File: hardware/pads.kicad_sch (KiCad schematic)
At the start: 56 parts, among them J1 5V, J10 5V, J11 5V, J12 5V, J13 5V, J14 5V, J15 5V, J16 5V, J17 5V, J18 5V, J19 5V, J2 5V, J20 5V, J21 5V, J22 5V, J23 5V, J24 5V, J25 5V, J26 5V, J27 5V, J28 5V, J29 5V, J3 5V, J30 5V, J31 5V, J32 5V, J33 5V, J34 5V, J35 5V, J36 5V, J37 5V, J38 5V, J39 5V, J4 5V, J40 5V, J41 5V, J42 5V, J43 5V, J44 5V, J45 5V, J46 5V, J47 5V, J48 5V, J49 5V, J5 5V, J50 5V, J51 5V, J52 5V, J53 5V, J54 5V, J6 5V, J7 5V, J8 5V, J9 5V, P1 SM08B-SRSS-TB(LF)(SN), U8 SM06B-SRSS-TB(LF)(SN)

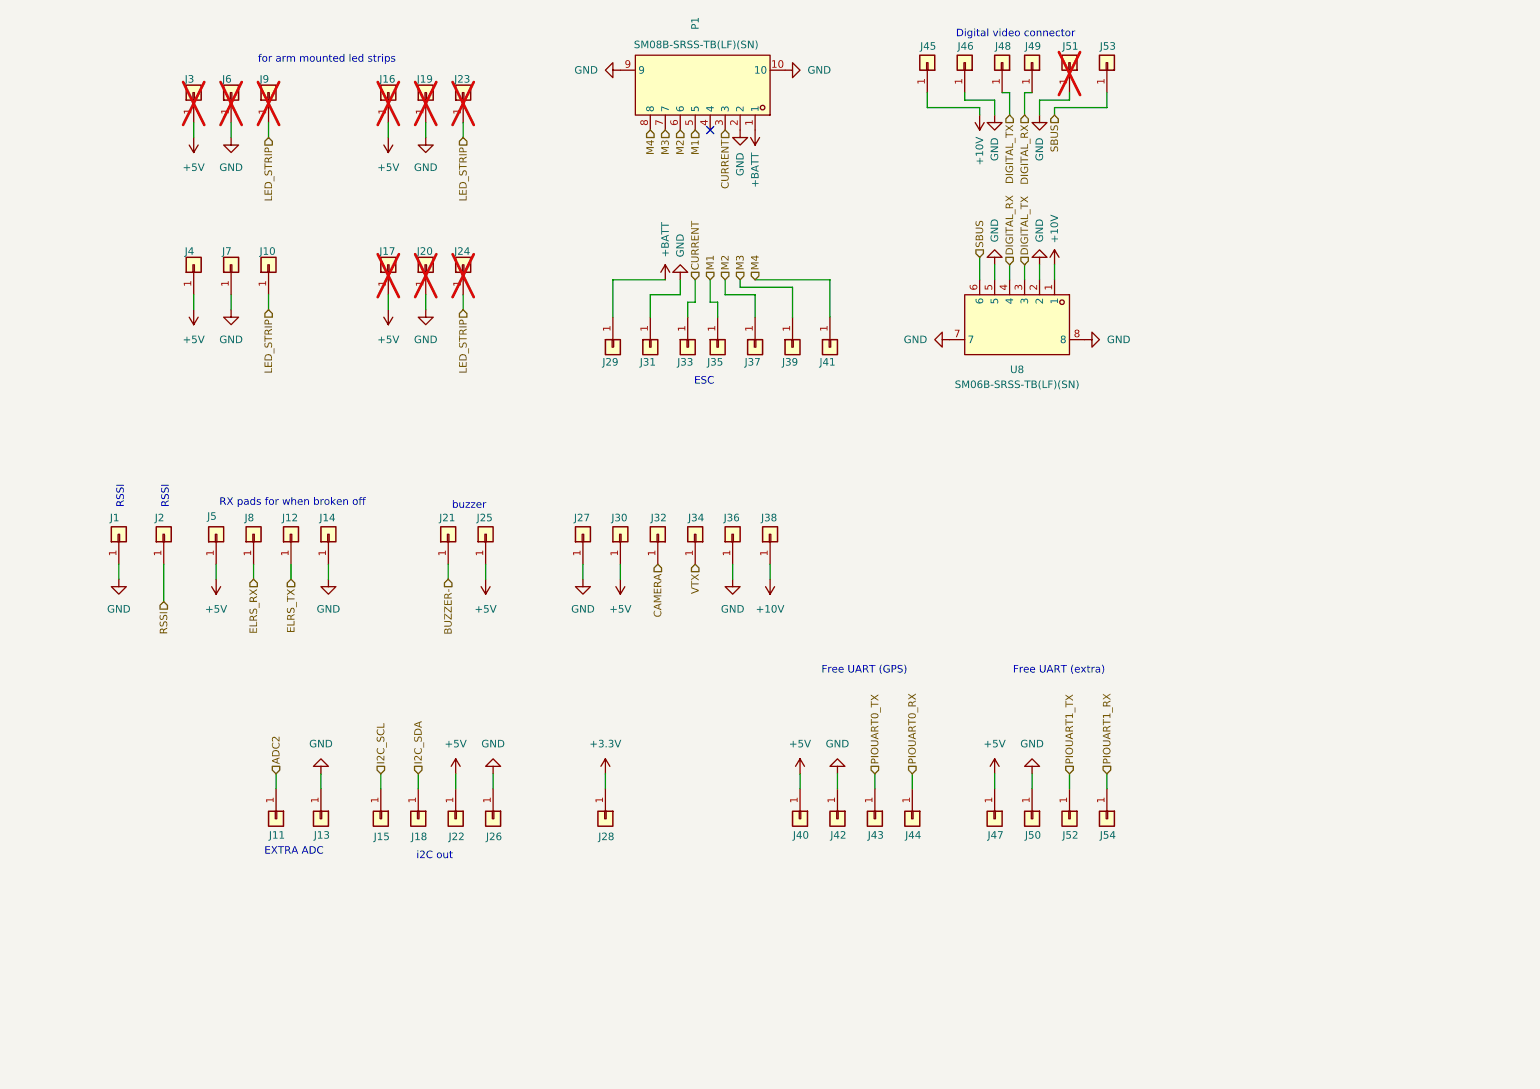
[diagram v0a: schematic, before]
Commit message: Rev 2 (RP2354A): finalize design, update docs, clean repo (#5)
* docs(readme): add analog OSD BOM to Rev 2 change list

Document OSD debugging findings and component changes as a new
Analog OSD section in the Rev 2 Change List:
- HW-12: U19 op-amp TLV9061IDPWR -> COS8051SOT (175MHz video-grade RRIO)
- HW-13: output front-end add AC-couple + DC-restore, power U19 from +5V
- HW-14: U20 comparator TLV3201AIDBVR -> TLV7031DPWR (push-pull, X2SON, ~75% smaller)
- HW-15: add OSD_EN select pull-down (datasheet-required, defaults to pass-through)
- U18 / D9 verified correct, no change; OSD GPIO mapping noted (PA4/5/6)

Also fix HW-11 beeper GPIO: GPIO6 -> GPIO7 (GPIO6 is OSD_SYNC per netlist).

Co-Authored-By: Claude Opus 4.8 (1M context) <noreply@anthropic.com>

* many tiny improvements

- I/O correctness
- SPI0/SPI1/I2C0 bus corrections
- decoupling of DVDD
- ADC_AVDD as per RPi documents
- removal of SBUS
- connect ESC serial
- remove RUN RC-circuit as per RPi documentation
- some more cleanup for readability
- gyro CLKIN decision
- I2C 4.7k pullup

* RP2354A

* piu1

* switch spi

* Update OpenFC.kicad_pcb

* routex2

* some minor tweaks

- remove some unnecessary resistors
- slightly higher 10V rail to account for voltage drop
- some cleanup
- simpler PG 1.8V circuit

* Update imu.kicad_sch

* LED resistors

Also reduced the amount of different resistors for cheaper assembly

* Delete leds.kicad_sch

* remove some unneeded decoupling caps from RP2350

* update MOSFET part numbers

* OSD

* ROUTE

* clean libs

* details

* led names

* Clean routing

* docs: rewrite README + CLAUDE.md for finalized Rev 2 (RP2354A)

Rev 2 is a substantial redesign that the docs no longer matched. Updated
both to the actual schematic, verified from the current netlist:

- MCU: RP2354B (QFN-80, GPIO0-47) -> RP2354A (QFN-60, GPIO0-29). Full GPIO
  map re-derived from the netlist + QFN-60 pinout; all 30 GPIO documented.
- IMU moved to SPI1, microSD to SPI0; ref designators re-annotated
  (op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
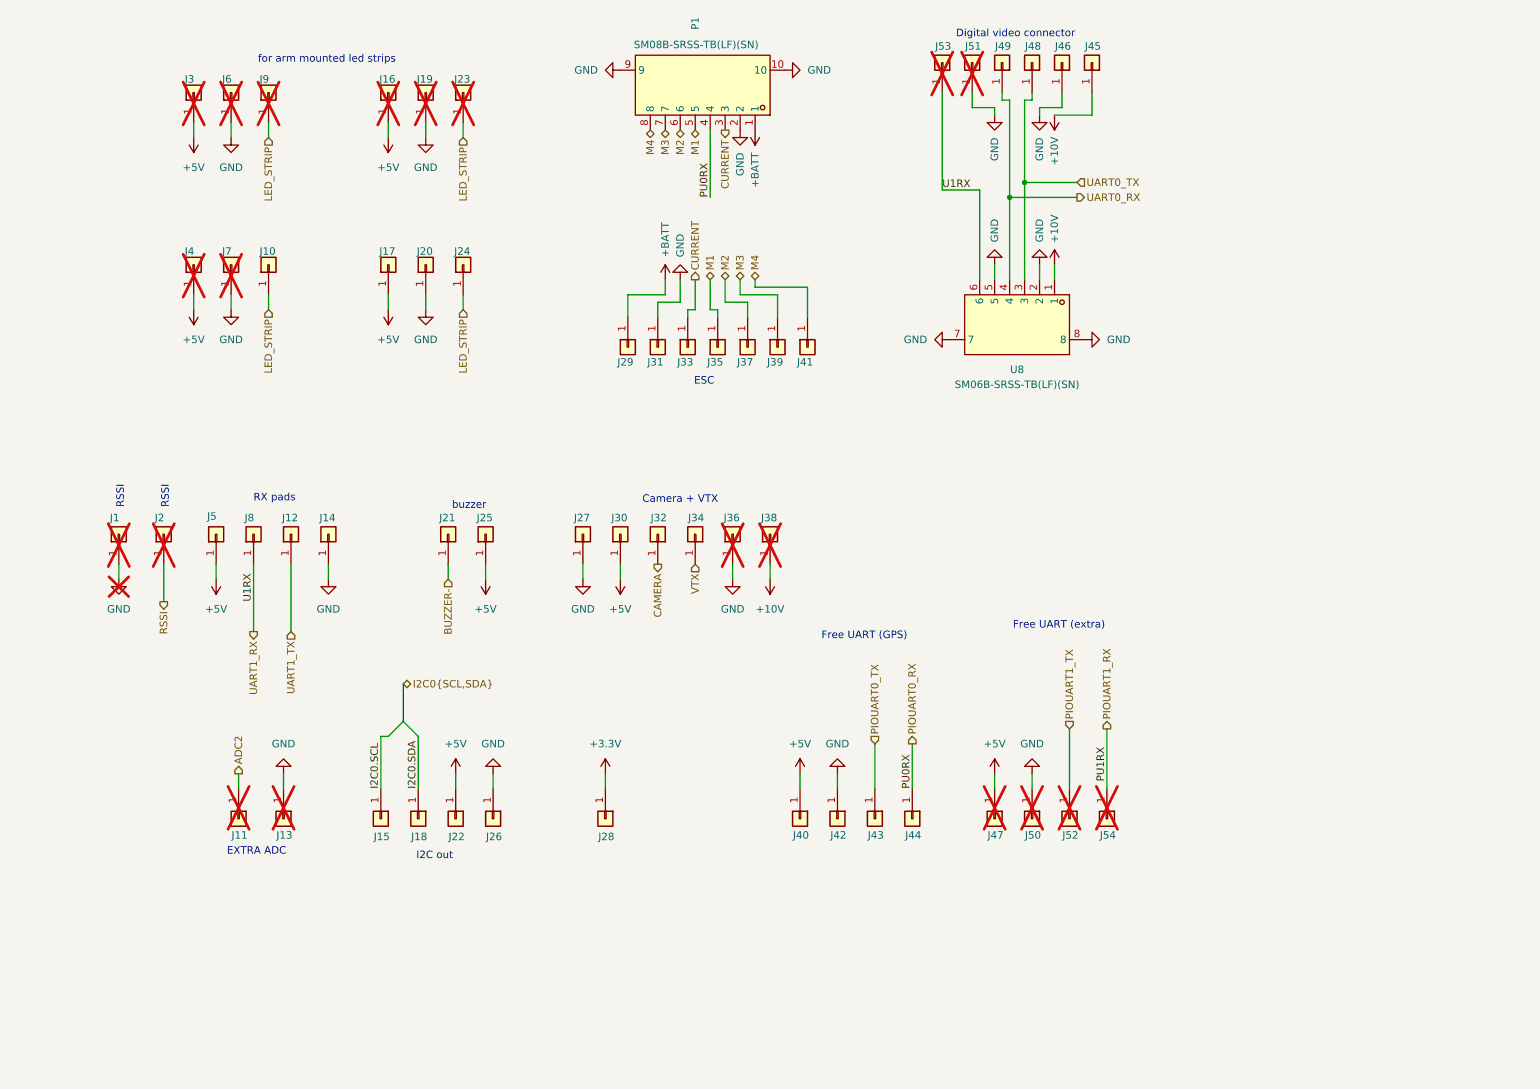
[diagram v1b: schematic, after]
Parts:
- J1, J11, J13, J2, J36, J38, J4, J47, J50, J52, J53, J54, J7: now not fitted
- J17, J20, J24: now fitted; now in the parts list
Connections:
- net SBUS is gone; now on net UART1_RX: J53.1 (Pin_1), U8.6
- net PIOUART0_RX: now also P1.4
- net DIGITAL_RX renamed UART0_RX
- net DIGITAL_TX renamed UART0_TX
- net ELRS_RX renamed UART1_RX
- net ELRS_TX renamed UART1_TX
- net I2C_SCL renamed I2C0.SCL
- net I2C_SDA renamed I2C0.SDA
- no-connect marks 1 -> 0
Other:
- note added: "Camera + VTX"
- note added: "I2C out"
- note added: "RX pads"
- note removed: "RX pads for when broken off"
- note removed: "i2C out"
- moved on the sheet: J29, J31, J37, J39, J41, J45, J46, J48, J49, J51

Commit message: docs(schematic): add design annotations to all sheets
Port on-canvas engineering comments from OpenFC-Lite (RP2354B), adapted to the
Mini layout. +41 text items across root, rp2350a, power, imu, osd, blackbox,
pads. Annotation/text only — no net or connectivity changes. Mirrors
hardware/DESIGN_NOTES.md.

Co-Authored-By: Claude Opus 4.8 (1M context) <noreply@anthropic.com>
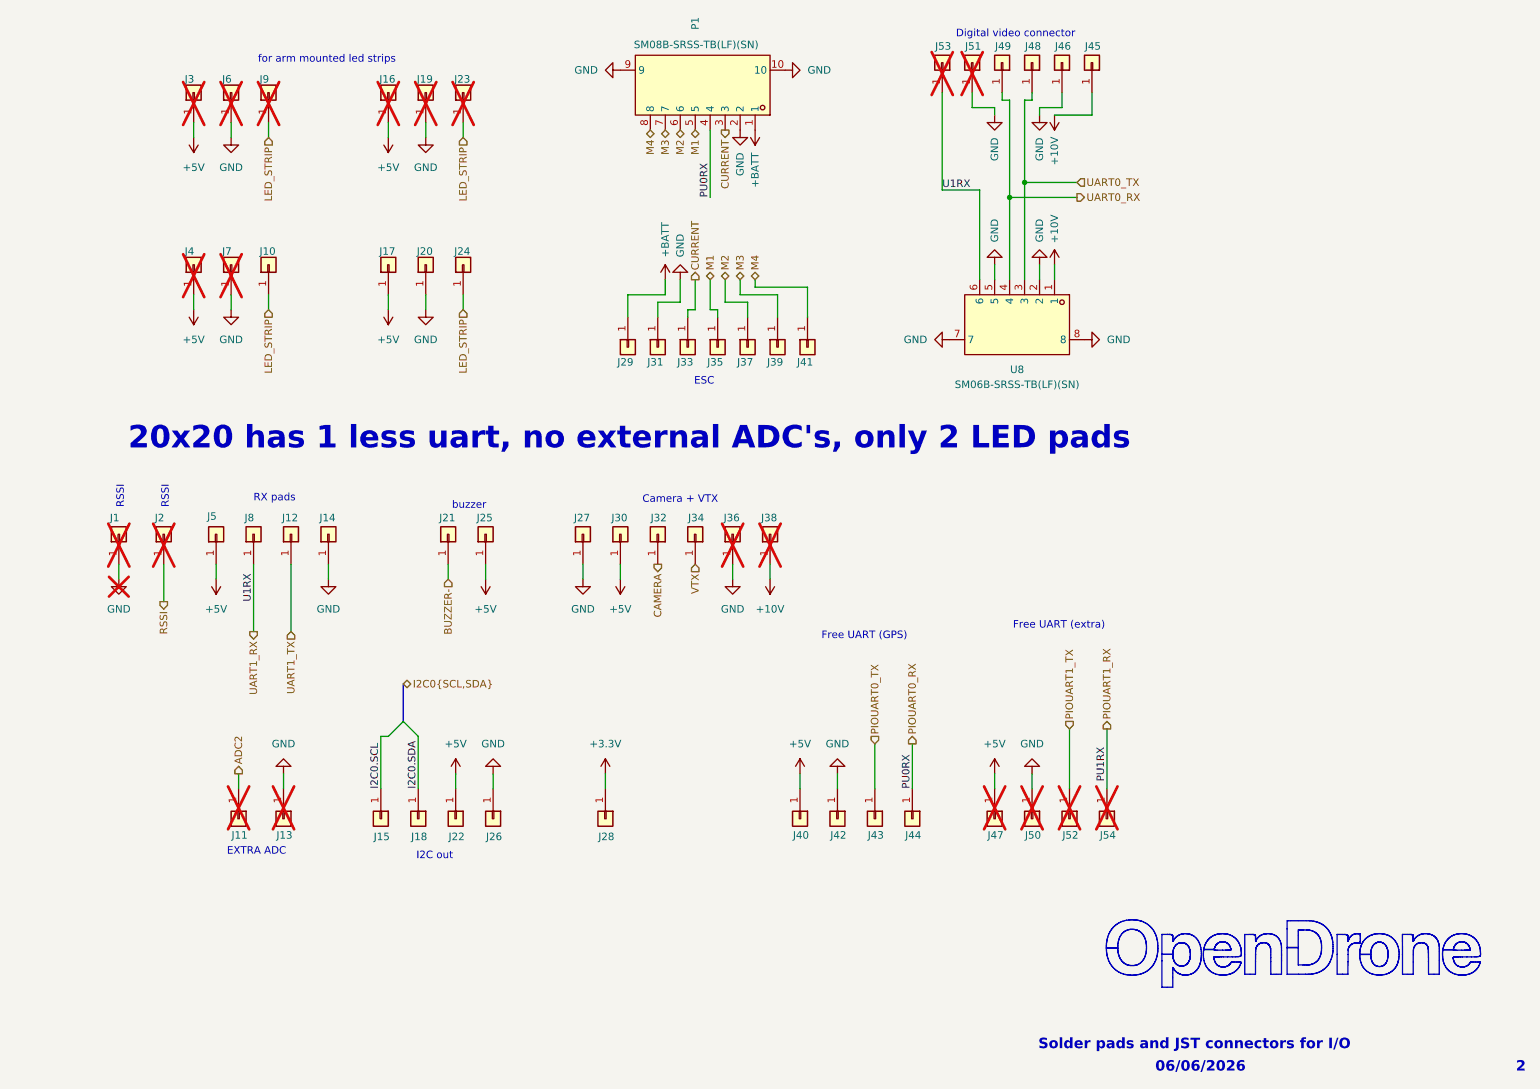
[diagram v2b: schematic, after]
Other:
- note added: "06/06/2026"
- note added: "2"
- note added: "20x20 has 1 less uart, no external ADC's, only 2 LED pads"
- note added: "Solder pads and JST connectors for I/O"

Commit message: chore(bom): consolidate LCSC Part -> LCSC field across schematic, library, footprints, project
Single canonical LCSC field (was split LCSC / LCSC Part). Every part resolves to one LCSC code; netlist verified, no duplicates. Includes Rev2 re-annotation resync re-save.

Co-Authored-By: Claude Opus 4.8 (1M context) <noreply@anthropic.com>
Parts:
- P1: LCSC (none) -> C160407; LCSC Part C160407 -> (none)
- U8: LCSC (none) -> C160405; LCSC Part C160405 -> (none)
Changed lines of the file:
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@@
 			)
 		)
-		(property "LCSC Part" "C160405"
+		(property "LCSC" "C160405"
 			(at 161.29 64.77 0)
 			(hide yes)
@@
 			)
 		)
-		(property "LCSC Part" "C160407"
+		(property "LCSC" "C160407"
 			(at 105.41 29.21 0)
 			(hide yes)
